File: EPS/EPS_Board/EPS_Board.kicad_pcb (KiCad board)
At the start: 2 copper layers, 100 x 100 mm, 15 parts, among them J1 Conn_02x02_Counter_Clockwise, J2 Conn_01x04_Female, J3 Conn_01x04_Female, J4 Conn_01x04_Female, J5 Conn_01x04_Female, J6 Conn_01x04_Female, U1 AZ1117-3.3, U2 AZ1117-3.3, U3 AZ1117-5.0, U4 AZ1117-5.0

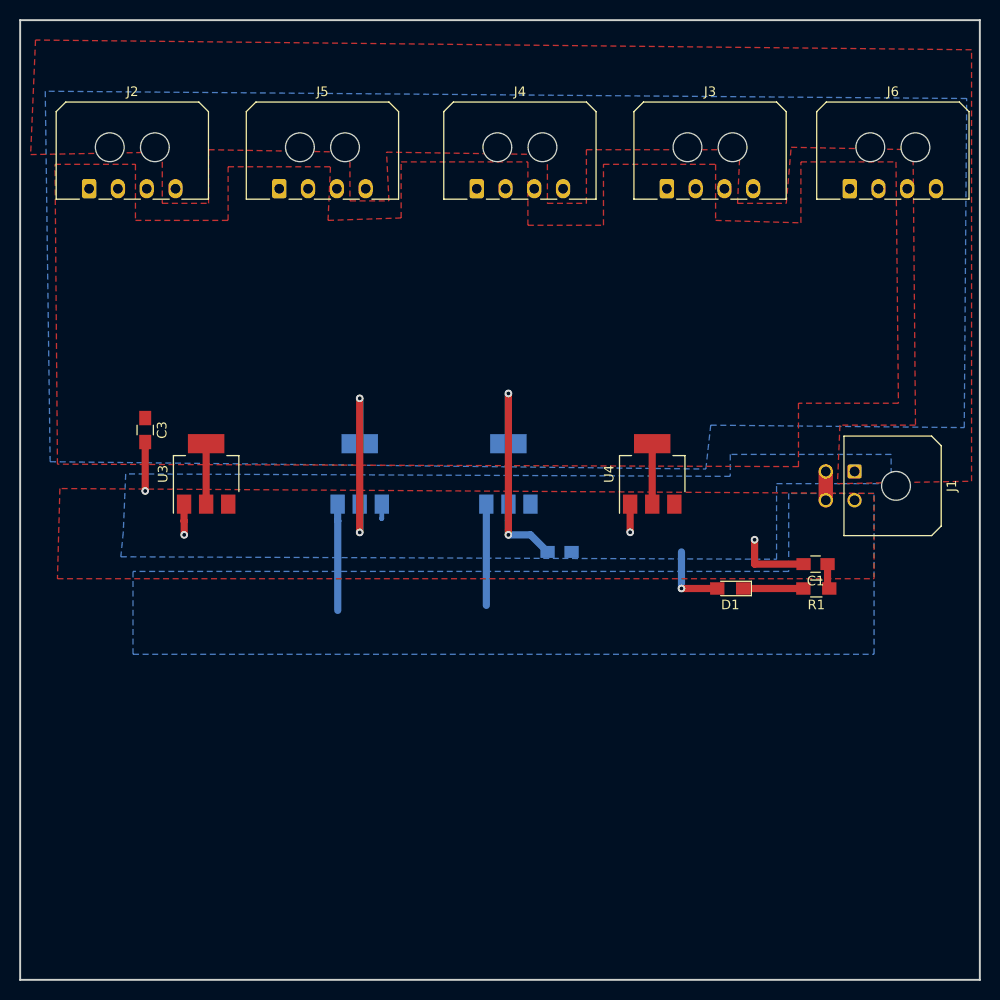
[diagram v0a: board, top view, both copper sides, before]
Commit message: Updated for individual caps for the linear regs.
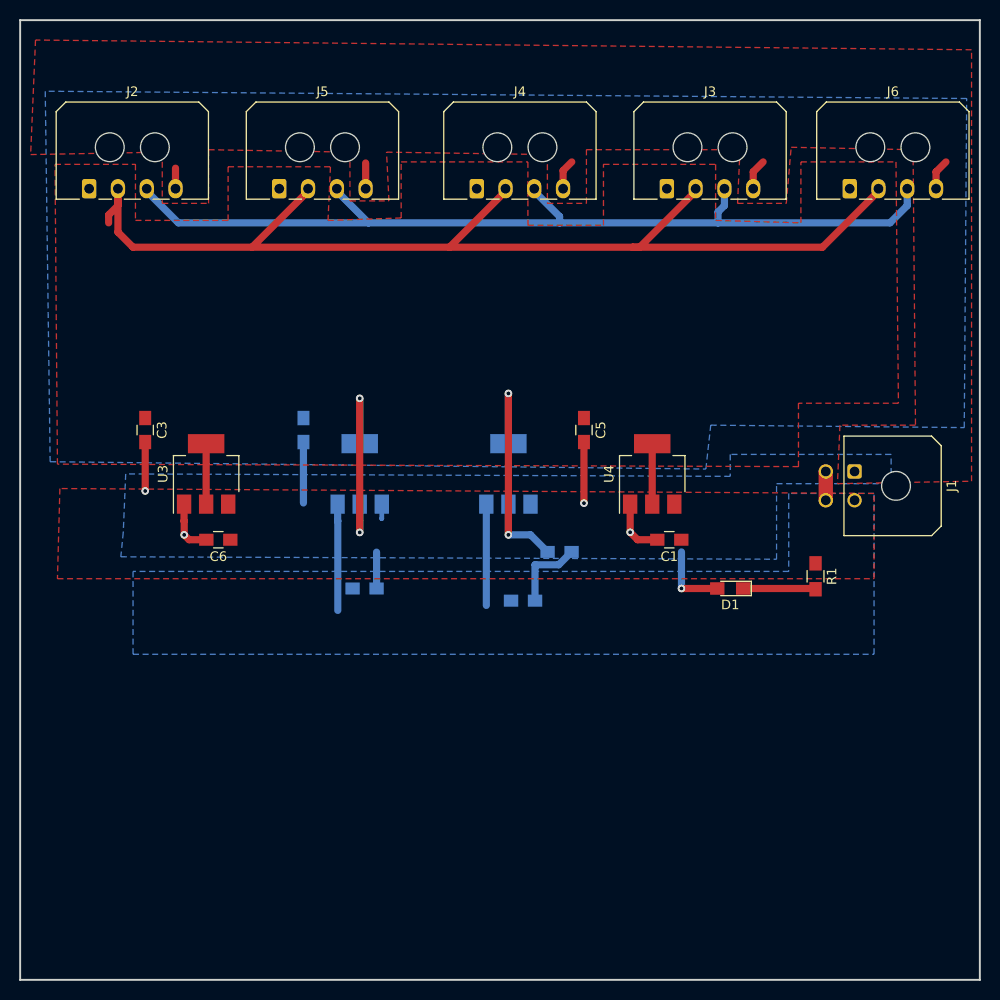
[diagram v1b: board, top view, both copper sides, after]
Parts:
- added C4: CAP, Capacitors_SMD:C_0805_HandSoldering, B.Cu at (129.5, 92.7)
- added C5: CAP, Capacitors_SMD:C_0805_HandSoldering, F.Cu at (158.8, 92.7)
- added C6: CAP, Capacitors_SMD:C_0805_HandSoldering, F.Cu at (120.7, 104.1)
- added C7: CAP, Capacitors_SMD:C_0805_HandSoldering, B.Cu at (152.4, 110.5)
- added C8: CAP, Capacitors_SMD:C_0805_HandSoldering, B.Cu at (135.9, 109.2)
- moved C1 15.5 mm to (167.6, 104.1)
- moved R1 1.27 mm to (182.9, 108.0), turned to 270 degrees
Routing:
- net +5V: track 14.1 -> 131.4 mm
- net +3V3: track 49.6 -> 146.4 mm
- net GND: track 27.9 -> 65.0 mm
- net +BATT: track 24.5 -> 21.6 mm
- net Net-(D1-Pad1): track 6.27 -> 7.57 mm
